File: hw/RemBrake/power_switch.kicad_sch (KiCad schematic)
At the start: 44 parts, among them Q1 SiS415DNT, Q2 BC337, Q3 BC847, Q4 BC337, Q5 BC847, U1 TPS62140, U2 BD48ExxG, U3 XC6220B331MR, U4 MAX40200AUK, U8 SG-107

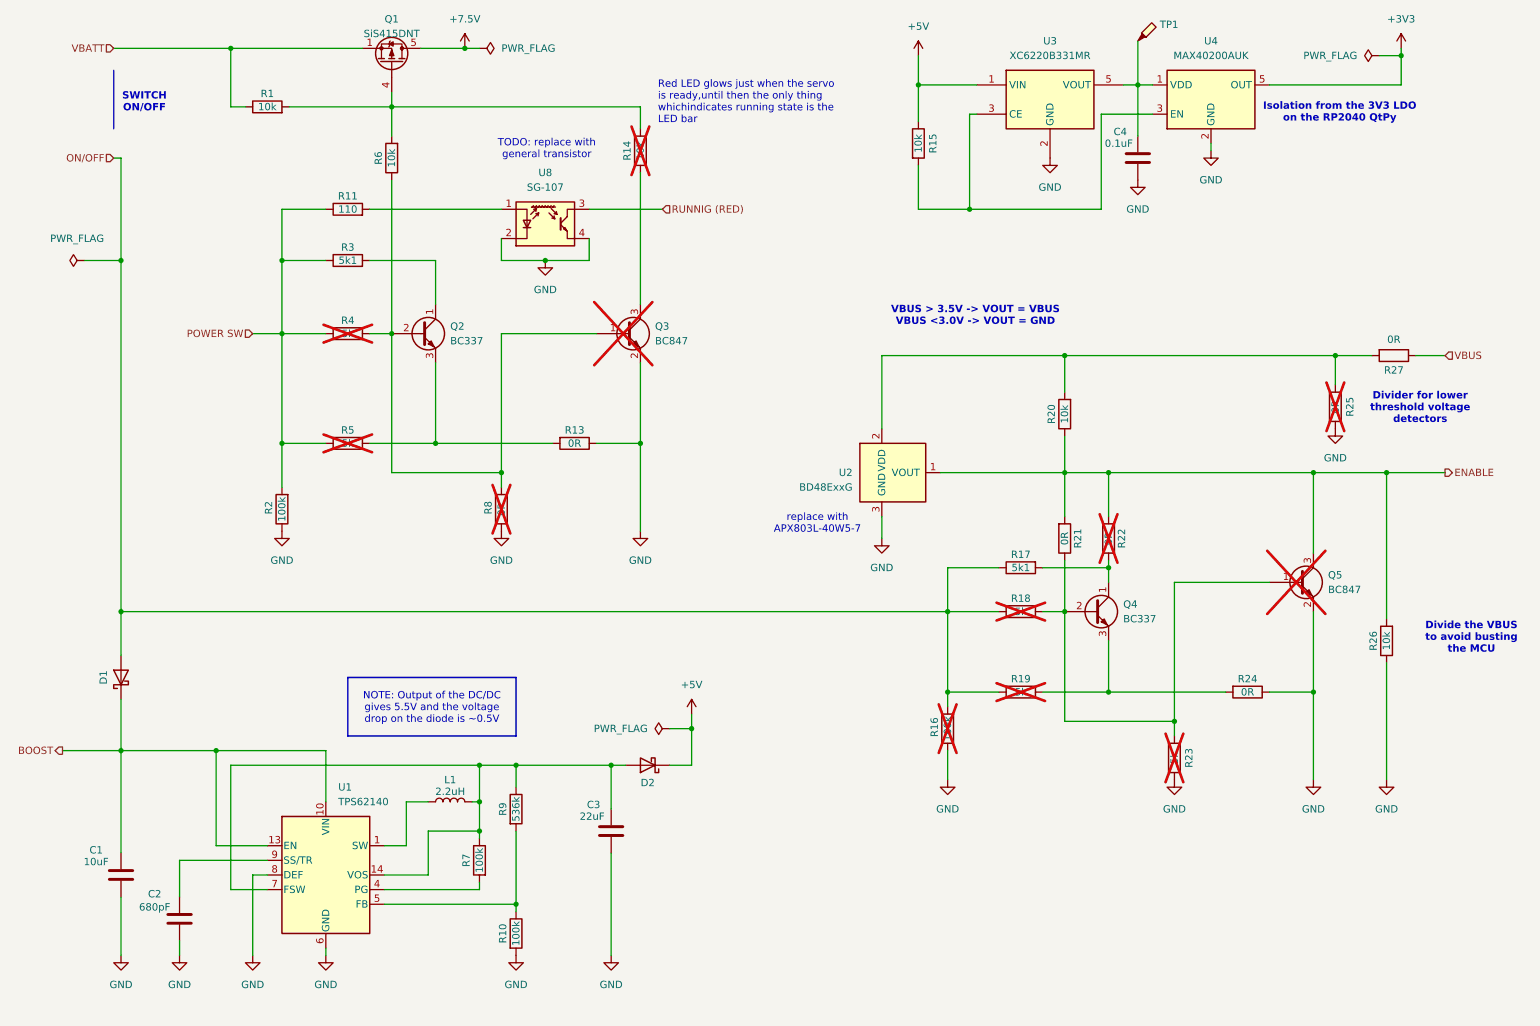
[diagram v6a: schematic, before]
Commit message: replaced optocoupler with transistor and loaded components in the pcb sheet
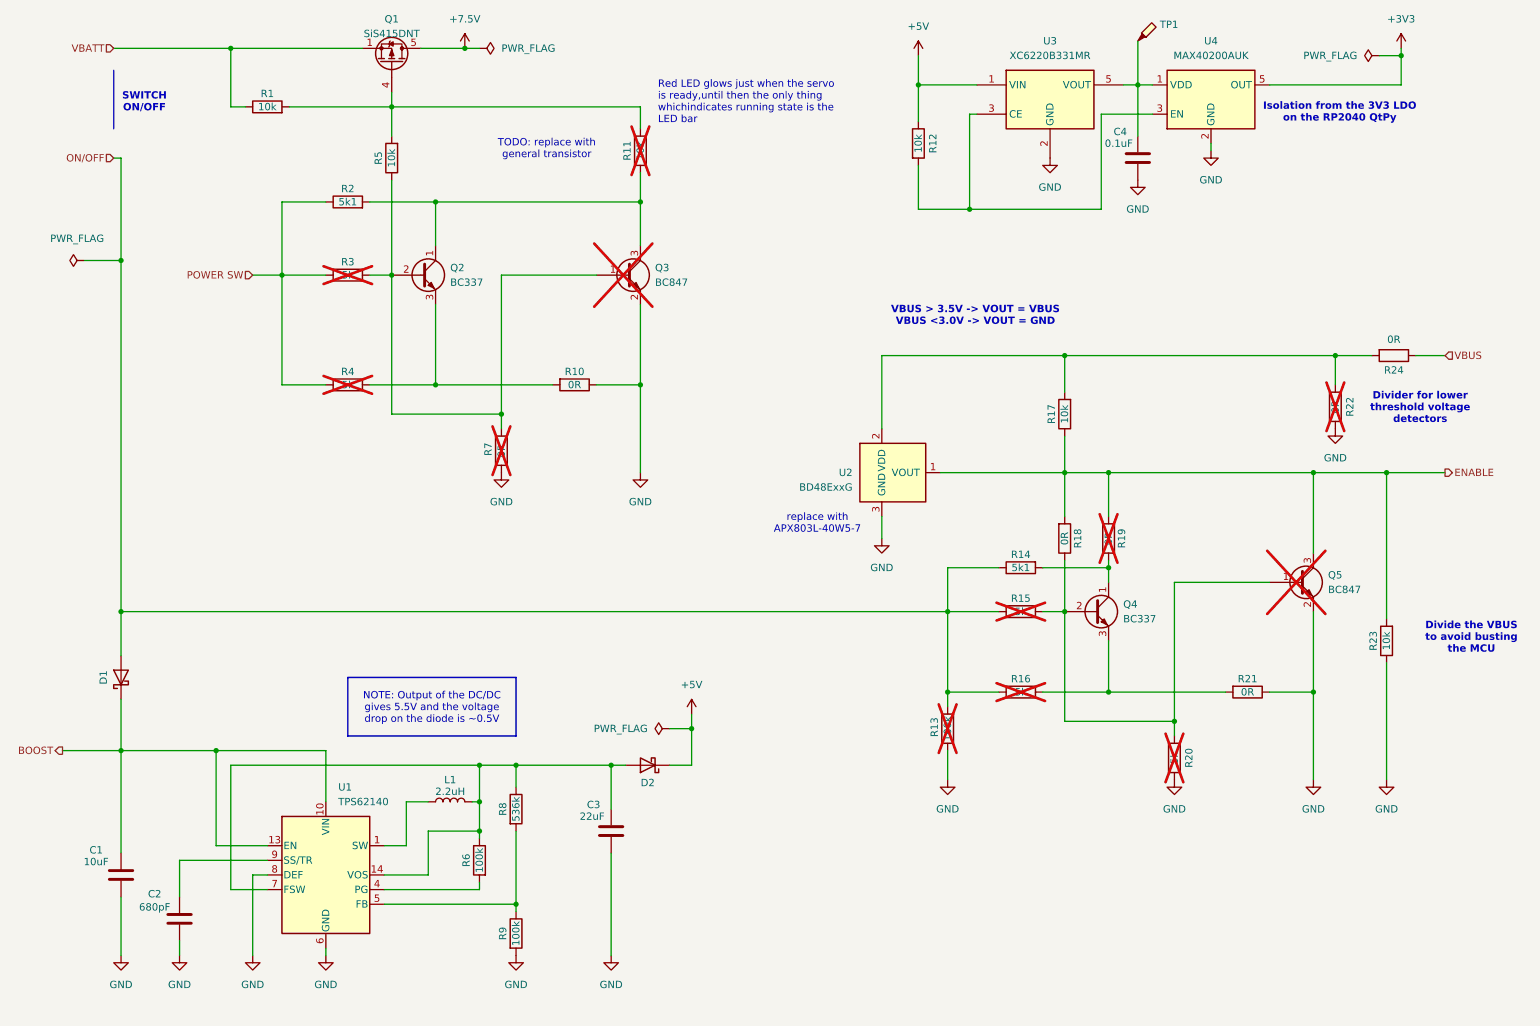
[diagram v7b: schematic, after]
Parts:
- removed R11: 110, Resistor_SMD:R_0805_2012Metric_Pad1.20x1.40mm_HandSolder, symbol Device:R
- removed R2: 100k, Resistor_SMD:R_0805_2012Metric_Pad1.20x1.40mm_HandSolder, symbol Device:R
- removed U8: SG-107, OptoDevice:Kodenshi_SG105, symbol Sensor_Proximity:SG-107
- renumbered R13 to R10, R14 to R11, R15 to R12, R16 to R13, R17 to R14, R18 to R15, R19 to R16, R20 to R17, R21 to R18, R22 to R19, R3 to R2, R23 to R20, R24 to R21, R25 to R22, R26 to R23, R27 to R24, R4 to R3, R5 to R4, R6 to R5, R7 to R6, R8 to R7, R9 to R8, R10 to R9
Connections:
- net at Q2.1 (C), R2.2: now also Q3.3 (C), R11.1
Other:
- moved on the sheet: Q2, Q3, R10, R2, R3, R4, R7

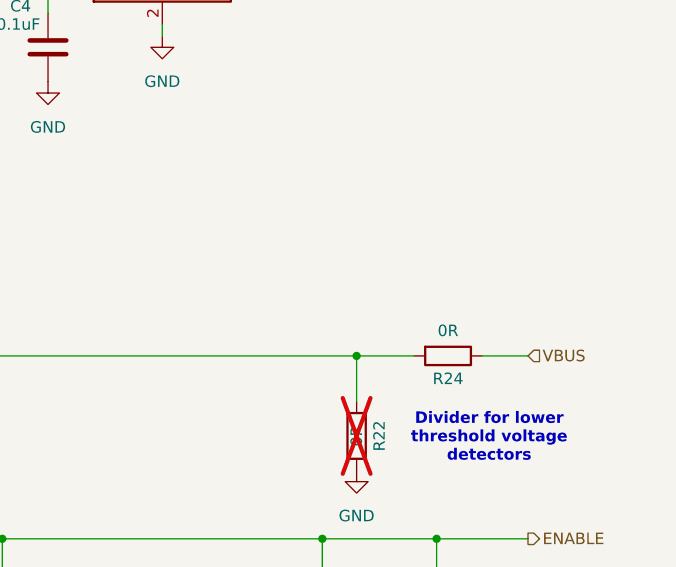
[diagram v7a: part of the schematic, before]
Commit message: version update and added missing connection between VBUS and 5V
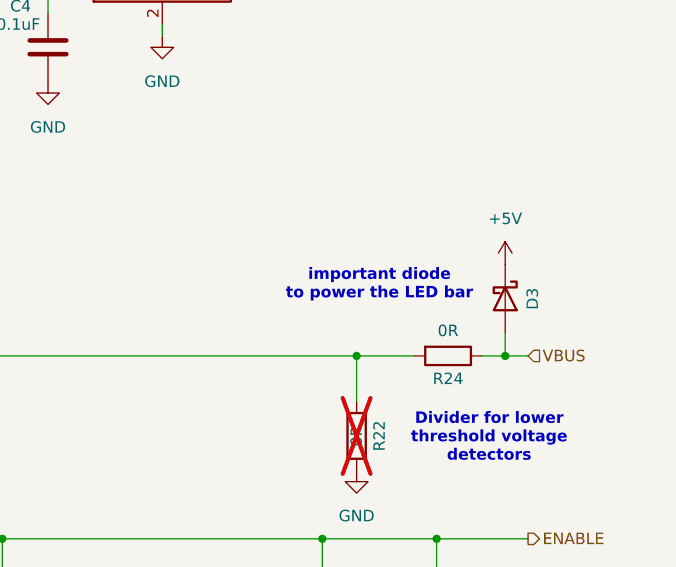
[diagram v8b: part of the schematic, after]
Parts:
- added D3: MBR0520, Diode_SMD:D_SOD-123, symbol Device:D_Schottky
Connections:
- net +5V: now also D3.1 (K)
- net VBUS: now also D3.2 (A)
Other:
- note added: "important diode to power the LED bar"
